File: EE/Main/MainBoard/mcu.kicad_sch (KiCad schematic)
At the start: 5 parts, among them J7 TAG_CONNECT, U1 STM32C011F4U6TR

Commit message: Random Check in
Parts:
- removed U1: STM32C011F4U6TR, Package_DFN_QFN:UQFN-20_3x3mm_P0.4mm, symbol New_Library:STM32C011F4U6TR
- added C10, C7, C9: 0.1u, Capacitor_SMD:C_0402_1005Metric, symbol Device:C
- added R3: 10k, Resistor_SMD:R_0402_1005Metric, symbol Device:R
- added TPDIN, TP_DIN_UP, TP_SCL, TP_SCL1: TestPoint, TestPoint:TestPoint_Pad_1.5x1.5mm, symbol Connector:TestPoint
- added U1: STM32F030F4Px, Package_SO:TSSOP-20_4.4x6.5mm_P0.65mm, symbol MCU_ST_STM32F0:STM32F030F4Px
- added U3: SN74LVC1T45DBV, Package_TO_SOT_SMD:SOT-23-6, symbol Logic_LevelTranslator:SN74LVC1T45DBV
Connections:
- net GND: now also C10.2, C7.2, C9.2, U1.15 (VSS), U3.2 (GND)
- net SCL: now also TP_SCL.1, U1.17 (PA9)
- net SDA: now also TP_SCL1.1, U1.18 (PA10)
- net SWDCLK: now also U1.20 (PA14)
- net SWDIO: now also U1.19 (PA13)
- net VCC: now also C7.1, C9.1, R3.1, U1.16 (VDD), U1.5 (VDDA), U3.1 (VCCA)
- new net: R3.2, U1.4 (NRST)
- new net DIR: U1.6 (PA0), U3.5 (DIR)
- new net DISPLAY_DIN: TPDIN.1, TP_DIN_UP.1, U1.13 (PA7), U3.3 (A), U3.4 (B)
- new net DNC_SPI_CLK: U1.11 (PA5)
- new net Vdrive: C10.1, U3.6 (VCCB)
- no-connect marks 5 -> 11
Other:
- moved on the sheet: R1, R2

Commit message: First pass layout
Assumes using Cut-through RGB 7 Segment
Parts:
- added R8, R9: 100k, Resistor_SMD:R_0402_1005Metric, symbol Device:R
- R3: value 10k -> 100k
- renumbered TPDIN to TPDIN1, TP_DIN_UP to TP_DIN_UP1, TP_SCL to TP_SCL2
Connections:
- net DIR: now also U1.2 (PF0); no longer U1.6 (PA0)
- net DISPLAY_DIN: no longer TP_DIN_UP1.1, U3.4 (B)
- net GND: now also R9.2
- net Start_00: now reaches U1.10 (PA4)
- net End: now reaches U1.14 (PB1)
- net Start_10: now reaches U1.3 (PF1)
- net Start_11: now reaches U1.8 (PA2)
- net Start_01: now reaches U1.9 (PA3)
- new net ADC: R8.2, R9.1, U1.6 (PA0)
- new net DISPLAY_DOUT: TP_DIN_UP1.1, U3.4 (B)
- new net VBAT_ADC: R8.1
- no-connect marks 11 -> 5

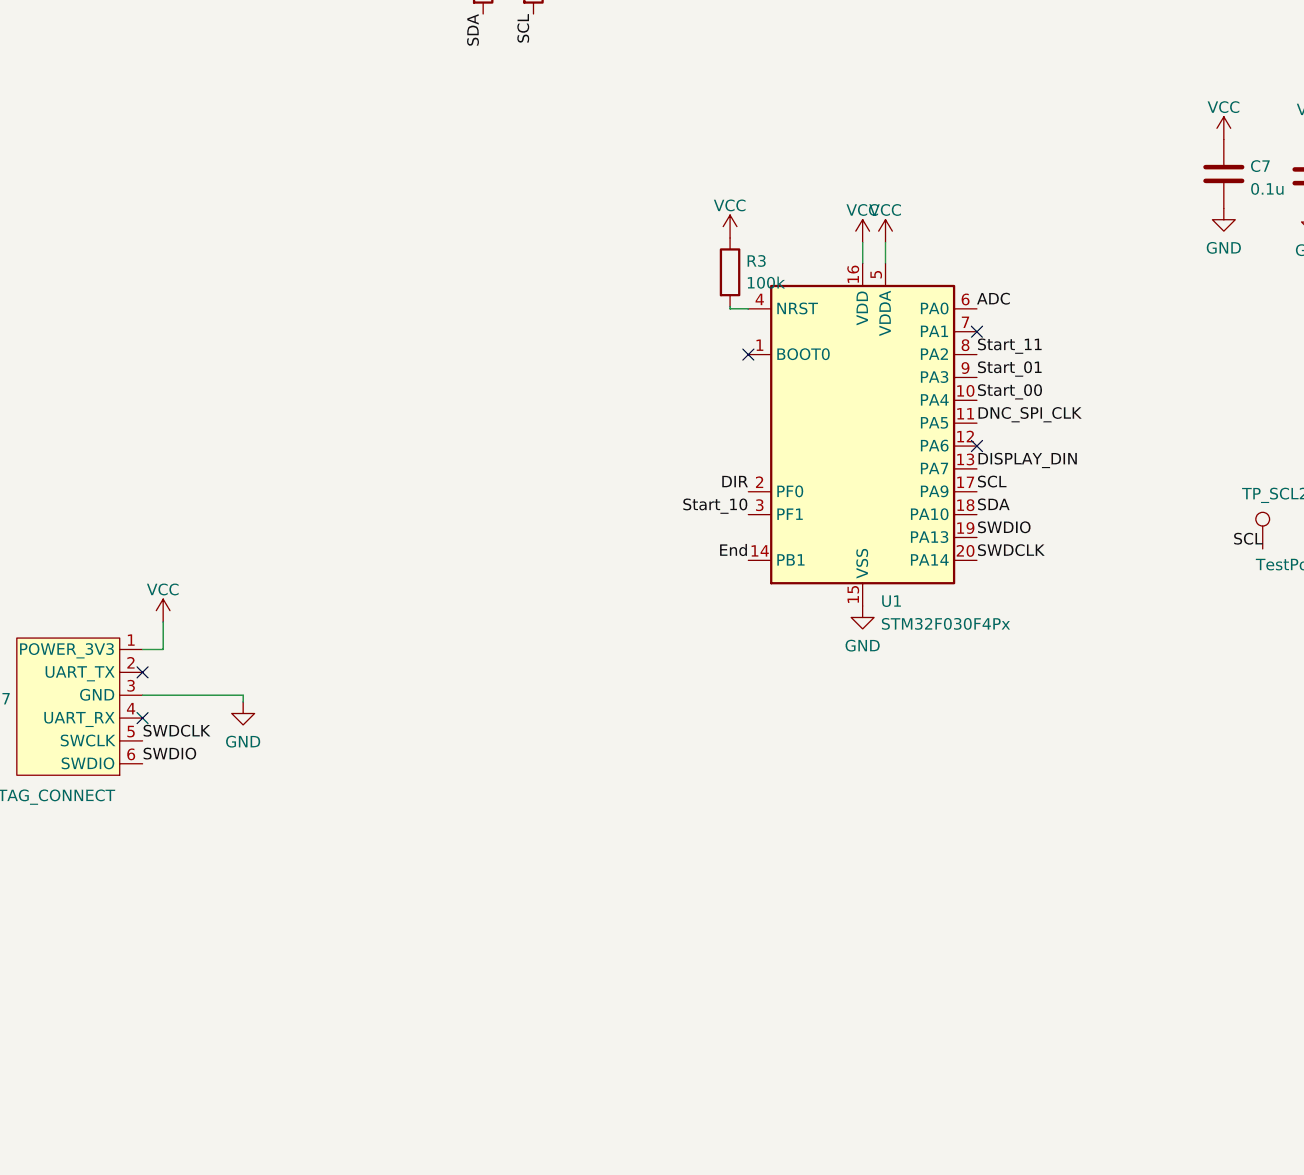
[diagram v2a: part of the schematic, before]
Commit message: MCU Modification
Migrated to g431, as is used elsewhere.
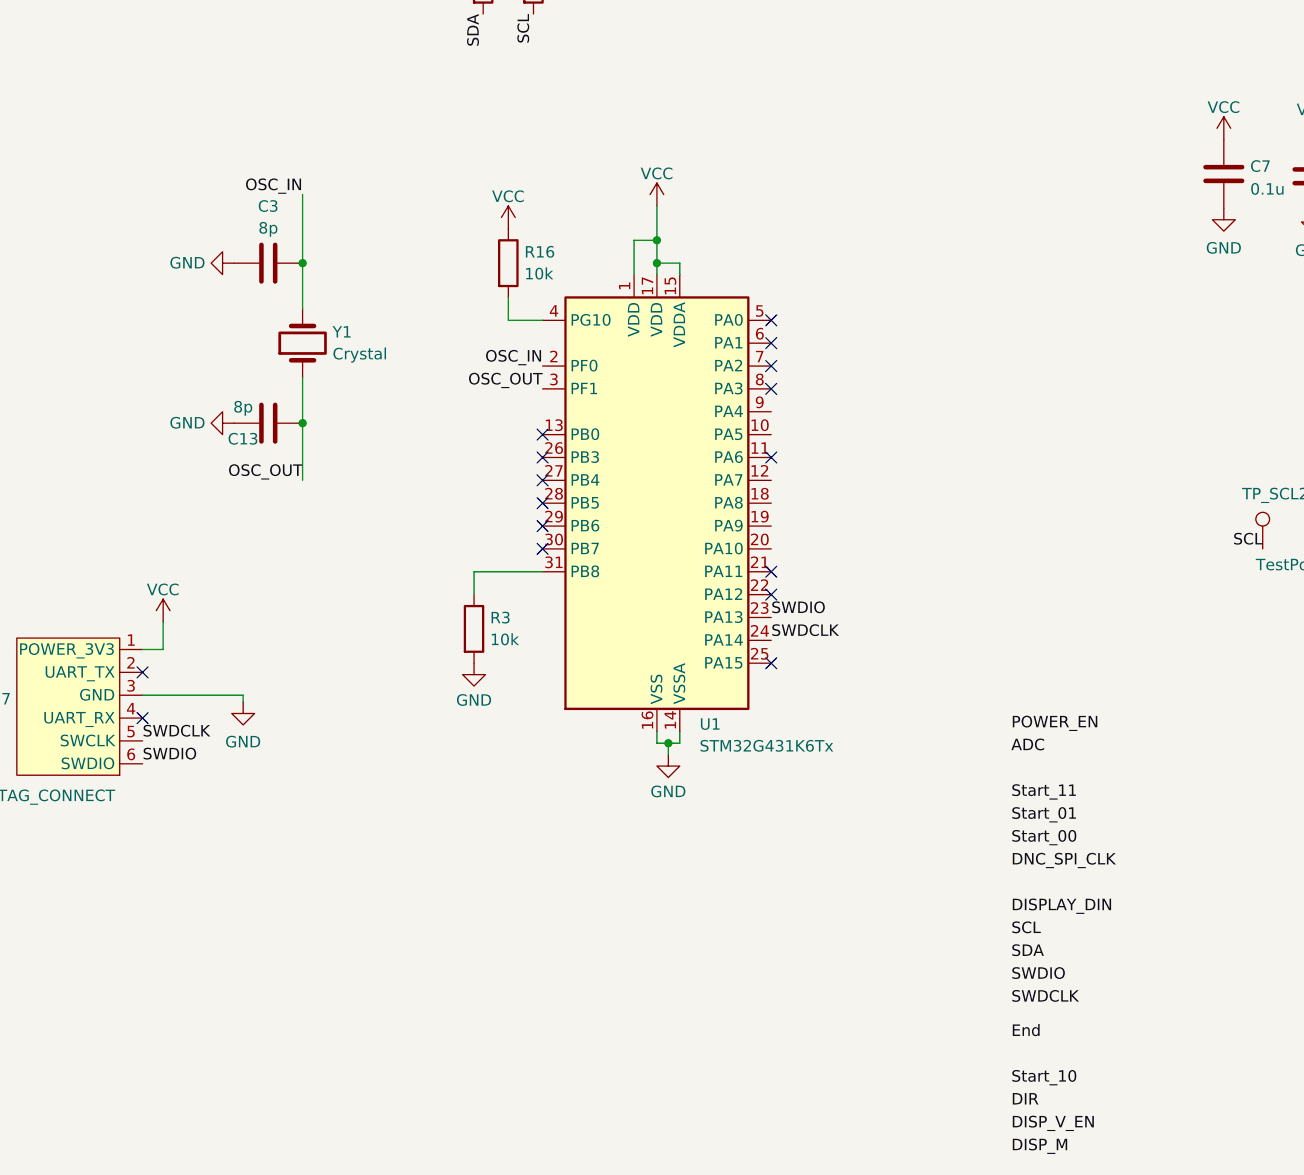
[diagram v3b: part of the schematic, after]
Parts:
- removed U1: STM32F030F4Px, Package_SO:TSSOP-20_4.4x6.5mm_P0.65mm, symbol MCU_ST_STM32F0:STM32F030F4Px
- added C13, C3: 8p, Capacitor_SMD:C_0402_1005Metric, symbol Device:C
- added R16: 10k, Resistor_SMD:R_0402_1005Metric, symbol Device:R
- added U1: STM32G431K6Tx, Package_QFP:LQFP-32_7x7mm_P0.8mm, symbol MCU_ST_STM32G4:STM32G431K6Tx
- added Y1: Crystal, Crystal:Crystal_SMD_5032-2Pin_5.0x3.2mm_HandSoldering, symbol Device:Crystal
- R3: value 100k -> 10k
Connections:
- net GND: now also R3.2, C13.1, C3.1, U1.14 (VSSA), U1.16 (VSS), U1.32 (VSS)
- net SWDCLK: now also U1.24 (PA14)
- net SWDIO: now also U1.23 (PA13)
- net VCC: now also R16.1, U1.1 (VDD), U1.15 (VDDA), U1.17 (VDD); no longer R3.1
- new net: R16.2, U1.4 (PG10)
- new net: R3.1, U1.31 (PB8)
- new net OSC_IN: C3.2, U1.2 (PF0), Y1.2
- new net OSC_OUT: C13.2, U1.3 (PF1), Y1.1
- no-connect marks 5 -> 16

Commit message: Potential Layout. Need to confirm button and L&F.
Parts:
- added R17, R19: 100k, Resistor_SMD:R_0402_1005Metric, symbol Device:R
- renumbered TP_SCL1 to TP_SDA1
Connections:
- net ADC: now also U1.5 (PA0)
- net DIR: now also R17.2, R19.1
- net DISPLAY_DIN: now also U1.30 (PB7)
- net End: now also U1.25 (PA15)
- net GND: now also R19.2
- net SCL: now also U1.19 (PA9)
- net SDA: now also U1.18 (PA8)
- net Start_00: now also U1.26 (PB3)
- net Start_01: now also U1.27 (PB4)
- net Start_10: now also U1.29 (PB6)
- net Start_11: now also U1.28 (PB5)
- net BAT_GATE: now reaches U1.12 (PA7)
- net BUTTON_EN: now reaches U1.13 (PB0)
- net DISP_EN: now reaches U1.8 (PA3)
- net VCC renamed +3V3
- net +3V3: now also R17.1
- no-connect marks 16 -> 2

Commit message: Potential Revision
Potentially fabb-able rev.
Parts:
- removed R17, R19: 100k, Resistor_SMD:R_0402_1005Metric, symbol Device:R
- removed TPDIN1, TP_DIN_UP1: TestPoint, TestPoint:TestPoint_Pad_1.5x1.5mm, symbol Connector:TestPoint
- removed U3: SN74LVC1T45DBV, Package_TO_SOT_SMD:SOT-23-6, symbol Logic_LevelTranslator:SN74LVC1T45DBV
- added C11, C5: C_NP, Capacitor_SMD:C_0402_1005Metric_Pad0.74x0.62mm_HandSolder, symbol Device:C
- added D2: LED, LED_SMD:LED_0603_1608Metric, symbol Device:LED
- added R20: 4.7k, Resistor_SMD:R_0402_1005Metric, symbol Device:R
- C10, C9: value 0.1u -> C_NP; footprint Capacitor_SMD:C_0402_1005Metric -> Capacitor_SMD:C_0402_1005Metric_Pad0.74x0.62mm_HandSolder
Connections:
- net DISPLAY_DIN is gone; now on net SDA: U1.30 (PB7)
- net DISP_EN is gone; now on net Start_11: U1.8 (PA3)
- net Vdrive is gone; now on net SCL: C10.1
- net +3V3: now also C5.1
- net ADC: now also U1.13 (PB0); no longer U1.5 (PA0)
- net BAT_GATE: now also U1.18 (PA8); no longer U1.12 (PA7)
- net BUTTON_EN: now also U1.9 (PA4); no longer U1.13 (PB0)
- net DISPLAY_DOUT: now also U1.12 (PA7)
- net End: now also U1.11 (PA6); no longer U1.25 (PA15)
- net GND: now also C11.2, R20.1; no longer C9.2
- net SCL: now also U1.25 (PA15), C5.2; no longer U1.19 (PA9)
- net SDA: now also C9.2, C11.1; no longer U1.18 (PA8)
- net Start_00: now also U1.5 (PA0); no longer U1.26 (PB3)
- net Start_01: now also U1.6 (PA1); no longer U1.27 (PB4)
- net Start_10: now also U1.7 (PA2); no longer U1.29 (PB6)
- net Start_11: no longer U1.28 (PB5)
- net DISPLAY_COUT: now reaches U1.10 (PA5)
- new net: D2.1 (K), R20.2
- new net HB: D2.2 (A), U1.26 (PB3)
- no-connect marks 2 -> 9
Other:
- note added: "These should be non populated caps. These pads will be sued to tune timing on the SCL/SDA lines for I2C, just in case the long traces become problematic."
- moved on the sheet: C1, C7

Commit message: Checkin of Fabbed Board
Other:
- note added: "TODO double check all nets"
- note added: "TODO double check pinouts here for I2C/SPI"
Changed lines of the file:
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@@
+		)
+	)
+	(text "TODO double check pinouts here for I2C/SPI"
+		(exclude_from_sim no)
+		(at 162.052 106.172 0)
+		(effects
+			(font
+				(size 1.27 1.27)
+			)
 		)
 	)
@@
 		(effects
 			(font
+				(size 1.27 1.27)
+			)
+		)
+	)
+	(text "TODO double check all nets"
+		(exclude_from_sim no)
+		(at 160.274 110.236 0)
+		(effects
+			(font
